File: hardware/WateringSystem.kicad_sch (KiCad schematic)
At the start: 0 parts

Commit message: Update KiCad hardware design files and improve gitignore
- Update KiCad PCB, schematic, and project files with latest changes
- Add KiCad project local settings file (WateringSystem.kicad_prl)
- Update symbol library table
- Improve .gitignore to exclude KiCad cache files and backup directories
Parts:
- added IC1: MAX485ESA+T, Samacsys:SOIC127P600X175-8N, symbol Samacsys:MAX485ESA+T
- added U1: ESP32-DEVKITC-32E, Snapeda:ESP32-DEVKITC-32E_MODULE_ESP32-DEVKITC-32E, symbol Snapeda:ESP32-DEVKITC-32E
- added U2: ~, Development_boards_custom:BME_280_qt_version, symbol Development_boards_custom:BME_280_qt_version

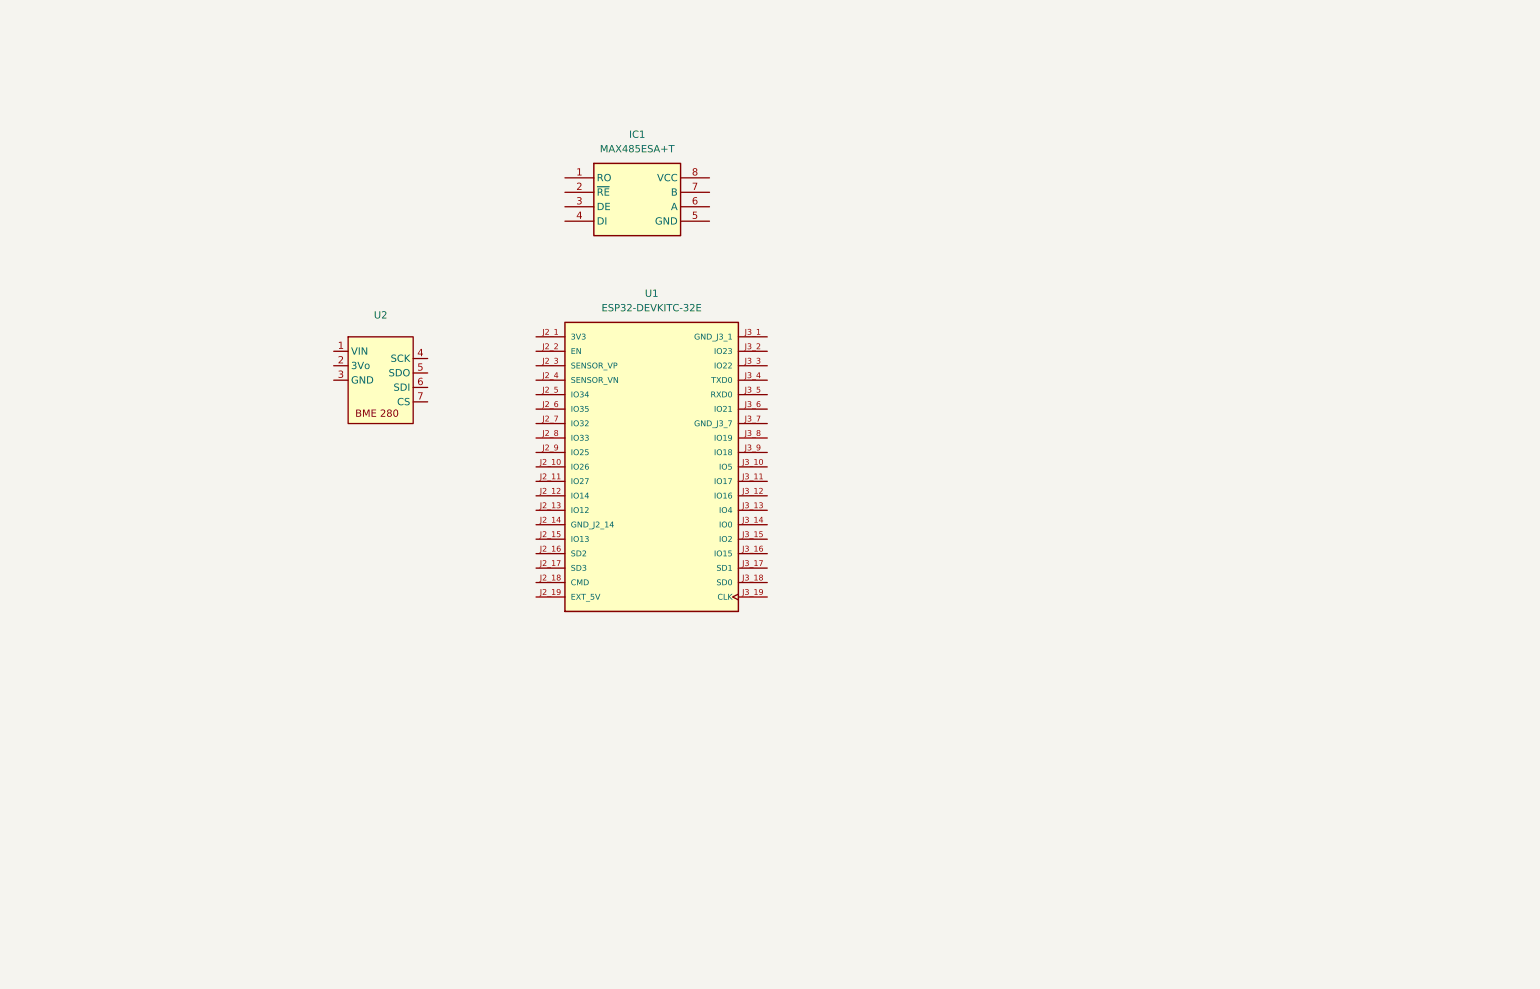
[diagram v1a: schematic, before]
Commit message: Uppdaterat KiCad-schema med TXS0108E och nätlista
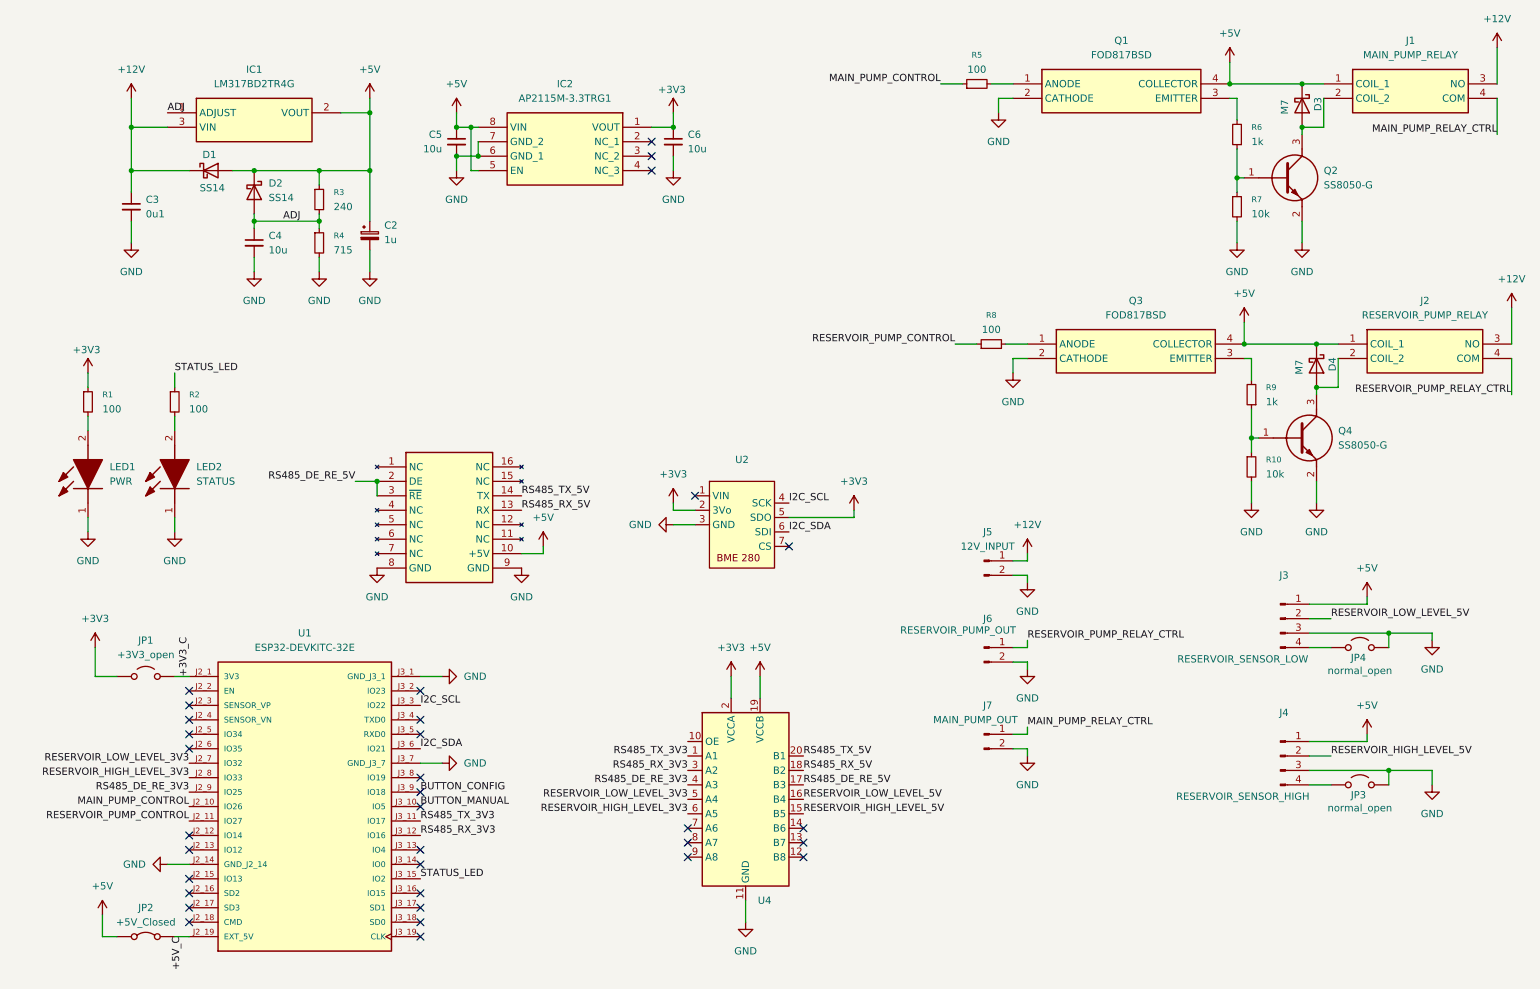
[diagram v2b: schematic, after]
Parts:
- removed IC1: MAX485ESA+T, Samacsys:SOIC127P600X175-8N, symbol Samacsys:MAX485ESA+T
- added Breakoutboard1: ~, Development_boards_custom:MAX485ESA+T_breakout, symbol Development_boards_custom:MAX485ESA+T
- added C2: 1u, Capacitor_Tantalum_SMD:CP_EIA-2012-12_Kemet-R, symbol Device:C_Polarized_Small
- added C3: 0u1, Capacitor_SMD:C_0805_2012Metric, symbol Device:C_Small
- added C4, C5, C6: 10u, Capacitor_SMD:C_0805_2012Metric, symbol Device:C_Small
- added D1, D2: SS14, Diode_SMD:D_SMA, symbol Device:D_Schottky
- added D3, D4: M7, Diode_SMD:D_SMA, symbol Device:D_Schottky
- added IC1: LM317BD2TR4G, Samacsys:LM317BD2TR4G, symbol Samacsys:LM317BD2TR4G
- added IC2: AP2115M-3.3TRG1, Samacsys:SOIC127P600X175-8N, symbol Samacsys:AP2115M-3.3TRG1
- added J1: MAIN_PUMP_RELAY, Samacsys:120715561, symbol Samacsys:1-2071556-1
- added J2: RESERVOIR_PUMP_RELAY, Samacsys:120715561, symbol Samacsys:1-2071556-1
- added J3: RESERVOIR_SENSOR_LOW, Connector_JST:JST_XH_B4B-XH-A_1x04_P2.50mm_Vertical, symbol Connector:Conn_01x04_Pin
- added J4: RESERVOIR_SENSOR_HIGH, Connector_JST:JST_XH_B4B-XH-A_1x04_P2.50mm_Vertical, symbol Connector:Conn_01x04_Pin
- added J5: 12V_INPUT, Samacsys:WEID_1715010000, symbol Samacsys:Weidmuller_1715010000
- added J6: RESERVOIR_PUMP_OUT, Samacsys:WEID_1715010000, symbol Samacsys:Weidmuller_1715010000
- added J7: MAIN_PUMP_OUT, Samacsys:WEID_1715010000, symbol Samacsys:Weidmuller_1715010000
- added JP1: +3V3_open, Jumper:SolderJumper-2_P1.3mm_Open_RoundedPad1.0x1.5mm, symbol Jumper:Jumper_2_Open
- added JP2: +5V_Closed, Jumper:SolderJumper-2_P1.3mm_Bridged_RoundedPad1.0x1.5mm, symbol Jumper:Jumper_2_Bridged
- added JP3, JP4: normal_open, Jumper:SolderJumper-2_P1.3mm_Open_RoundedPad1.0x1.5mm, symbol Jumper:Jumper_2_Open
- added LED1: PWR, Samacsys:150080SS75000, symbol Samacsys:150080SS75000
- added LED2: STATUS, Samacsys:LEDC2012X80N, symbol Samacsys:150080VS75000
- added Q1, Q3: FOD817BSD, Samacsys:SOP254P1016X385-4N, symbol Samacsys:FOD817BSD
- added Q2, Q4: SS8050-G, Samacsys:SOT95P240X115-3N, symbol Samacsys:SS8050-G
- added R1, R2, R5, R8: 100, Resistor_SMD:R_0805_2012Metric, symbol Device:R_Small
- added R10, R7: 10k, Resistor_SMD:R_0805_2012Metric, symbol Device:R_Small
- added R3: 240, Resistor_SMD:R_0805_2012Metric, symbol Device:R_Small
- added R4: 715, Resistor_SMD:R_0805_2012Metric, symbol Device:R_Small
- added R6, R9: 1k, Resistor_SMD:R_0805_2012Metric, symbol Device:R_Small
- added U4: ~, Development_boards_custom:TXS10108E_breakout, symbol Development_boards_custom:TXS1018E_breakout
- U1: footprint Snapeda:ESP32-DEVKITC-32E_MODULE_ESP32-DEVKITC-32E -> Snapeda:ESP32-DEVKITC-32E_MODULE_ESP32-DEVKITC-32E-for headers
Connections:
- net +3V3_C: now reaches U1.J2_1 (3V3)
- net +3V3_C: now also JP1.2 (B)
- net MAIN_PUMP_CONTROL: now reaches U1.J2_10 (IO26)
- net MAIN_PUMP_CONTROL: now also R5.1
- net RESERVOIR_PUMP_CONTROL: now reaches U1.J2_11 (IO27)
- net RESERVOIR_PUMP_CONTROL: now also R8.1
- net GND: now reaches U1.J2_14 (GND_J2_14)
- net GND: now also U1.J3_1 (GND_J3_1), U1.J3_7 (GND_J3_7), U2.3 (GND), Breakoutboard1.8 (GND), Breakoutboard1.9 (GND), C2.2, C3.2, C4.2, C5.2, C6.2, IC2.6 (GND_1), IC2.7 (GND_2), J3.3 (Pin_3), J4.3 (Pin_3), J5.2 (Pin_2), J6.2 (Pin_2), J7.2 (Pin_2), JP3.2 (B), JP4.2 (B), LED1.1 (K), LED2.1 (K), Q1.2 (CATHODE), Q2.2 (E), Q3.2 (CATHODE), Q4.2 (E), R10.2, R4.2, R7.2, U4.11 (GND)
- net +5V_C: now reaches U1.J2_19 (EXT_5V)
- net +5V_C: now also JP2.2 (B)
- net RESERVOIR_LOW_LEVEL_3V3: now reaches U1.J2_7 (IO32)
- net RESERVOIR_LOW_LEVEL_3V3: now also U4.5 (A4)
- net RESERVOIR_HIGH_LEVEL_3V3: now reaches U1.J2_8 (IO33)
- net RESERVOIR_HIGH_LEVEL_3V3: now also U4.6 (A5)
- net RS485_DE_RE_3V3: now reaches U1.J2_9 (IO25)
- net RS485_DE_RE_3V3: now also U4.4 (A3)
- net BUTTON_MANUAL: now reaches U1.J3_10 (IO5)
- net RS485_TX_3V3: now reaches U1.J3_11 (IO17)
- net RS485_TX_3V3: now also U4.1 (A1)
- net RS485_RX_3V3: now reaches U1.J3_12 (IO16)
- net RS485_RX_3V3: now also U4.3 (A2)
- net STATUS_LED: now reaches U1.J3_15 (IO2)
- net STATUS_LED: now also R2.1
- net I2C_SCL: now reaches U1.J3_3 (IO22)
- net I2C_SCL: now also U2.4 (SCK)
- net I2C_SDA: now reaches U1.J3_6 (IO21)
- net I2C_SDA: now also U2.6 (SDI)
- net BUTTON_CONFIG: now reaches U1.J3_9 (IO18)
- net +3V3: now reaches U2.2 (3Vo)
- net +3V3: now also U2.5 (SDO), C6.1, IC2.1 (VOUT), JP1.1 (A), R1.1, U4.2 (VCCA)
- new net: LED2.2 (A), R2.2
- new net: LED1.2 (A), R1.2
- new net: Q1.1 (ANODE), R5.2
- new net: Q1.3 (EMITTER), R6.2
- new net: J4.4 (Pin_4), JP3.1 (A)
- new net: J3.4 (Pin_4), JP4.1 (A)
- new net: Q3.1 (ANODE), R8.2
- new net: Q3.3 (EMITTER), R9.2
- new net: D4.2 (A), J2.2 (COIL_2), Q4.3 (C)
- new net: Q4.1 (B), R10.1, R9.1
- new net: Q2.1 (B), R6.1, R7.1
- new net: D3.2 (A), J1.2 (COIL_2), Q2.3 (C)
- new net +12V: C3.1, D1.1 (K), IC1.3 (VIN), J1.3 (NO), J2.3 (NO), J5.1 (Pin_1)
- new net +5V: Breakoutboard1.10 (+5V), C2.1, C5.1, D1.2 (A), D2.1 (K), D3.1 (K), D4.1 (K), IC1.2 (VOUT), IC2.5 (EN), IC2.8 (VIN), J1.1 (COIL_1), J2.1 (COIL_1), J3.1 (Pin_1), J4.1 (Pin_1), JP2.1 (A), Q1.4 (COLLECTOR), Q3.4 (COLLECTOR), R3.1, U4.19 (VCCB)
- new net ADJ: C4.1, D2.2 (A), IC1.1 (ADJUST), R3.2, R4.1
- new net MAIN_PUMP_RELAY_CTRL: J1.4 (COM), J7.1 (Pin_1)
- new net RESERVOIR_HIGH_LEVEL_5V: J4.2 (Pin_2), U4.15 (B5)
- new net RESERVOIR_LOW_LEVEL_5V: J3.2 (Pin_2), U4.16 (B4)
- new net RESERVOIR_PUMP_RELAY_CTRL: J2.4 (COM), J6.1 (Pin_1)
- new net RS485_DE_RE_5V: Breakoutboard1.2 (DE), Breakoutboard1.3 (~{RE}), U4.17 (B3)
- new net RS485_RX_5V: Breakoutboard1.13 (RX), U4.18 (B2)
- new net RS485_TX_5V: Breakoutboard1.14 (TX), U4.20 (B1)
- no-connect marks 0 -> 34
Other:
- title: (none) -> Watering System Breakout board
- moved on the sheet: U1, U2

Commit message: hardware: commit April design work — schematic pin fixes, PCB layout session, rev2 BOM (THVD1426), JLCPCB production files
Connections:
- net +3V3: now also U4.1 (VCCA), U4.10 (OE); no longer U4.2 (VCCA)
- net +5V: now also U4.20 (VCCB); no longer U4.19 (VCCB)
- net RS485_TX_3V3: now also U4.2 (A1); no longer U4.1 (A1)
- net RS485_TX_5V: now also U4.19 (B1); no longer U4.20 (B1)
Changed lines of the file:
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@@
 	(wire
 		(pts
+			(xy 130.81 147.32) (xy 132.08 147.32)
+		)
+		(stroke
+			(width 0)
+			(type default)
+		)
+	)
+	(wire
+		(pts
 			(xy 262.89 152.4) (xy 255.27 152.4)
 		)
@@
 	(wire
 		(pts
+			(xy 130.81 144.78) (xy 130.81 147.32)
+		)
+		(stroke
+			(width 0)
+			(type default)
+		)
+	)
+	(wire
+		(pts
 			(xy 41.91 90.17) (xy 41.91 92.71)
 		)
@@
 					(unit 1)
 				)
+			)
+		)
+	)
+	(symbol
+		(lib_id "power:+3V3")
+		(at 130.81 144.78 0)
+		(unit 1)
+		(exclude_from_sim no)
+		(in_bom yes)
+		(on_board yes)
+		(dnp no)
+		(fields_autoplaced yes)
+		(property "Reference" "#PWR046"
+			(at 130.81 148.59 0)
+			(effects
+				(font
+					(size 1.27 1.27)
+				)
+				(hide yes)
+			)
+		)
+		(property "Value" "+3V3"
+			(at 130.81 139.7 0)
+			(effects
+				(font
+					(size 1.27 1.27)
+				)
+			)
+		)
+		(property "Footprint" ""
+			(at 130.81 144.78 0)
+			(effects
+				(font
+					(size 1.27 1.27)
+				)
+				(hide yes)
+			)
+		)
+		(property "Datasheet" ""
+			(at 130.81 144.78 0)
+			(effects
+				(font
+					(size 1.27 1.27)
+				)
+				(hide yes)
+			)
+		)
+		(property "Description" "Power symbol creates a global label with name \"+3V3\""
+			(at 130.81 144.78 0)
+			(effects
+				(font
+					(size 1.27 1.27)
+				)
+				(hide yes)
+			)
+		)
+		(pin "1"
+		)
+		(instances
+			(project "WateringSystem"
+				(path "/48c2e22f-8006-434e-86fa-459a1d38947a"
+					(reference "#PWR046")
+					(unit 1)
+				)
